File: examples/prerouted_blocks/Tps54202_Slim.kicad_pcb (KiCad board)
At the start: 2 copper layers, 9 parts

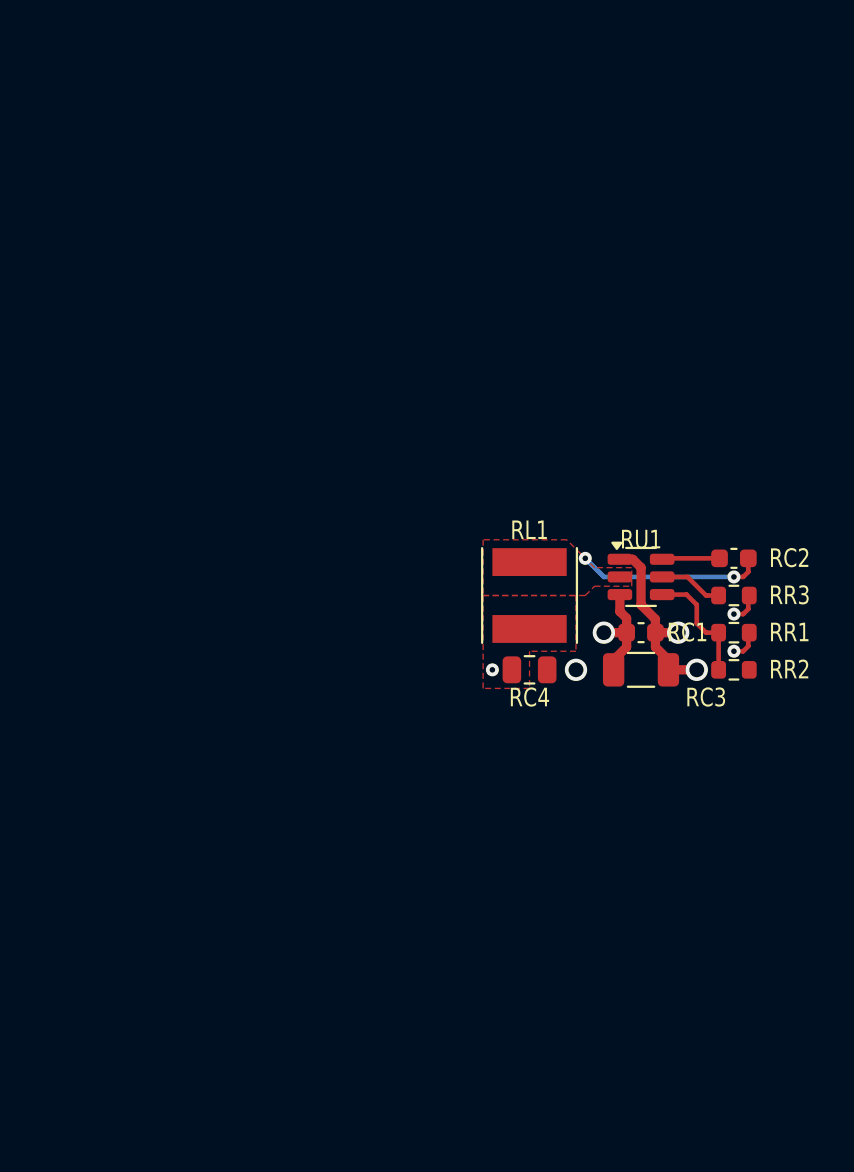
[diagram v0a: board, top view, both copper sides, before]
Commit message: clean up prerouted examples
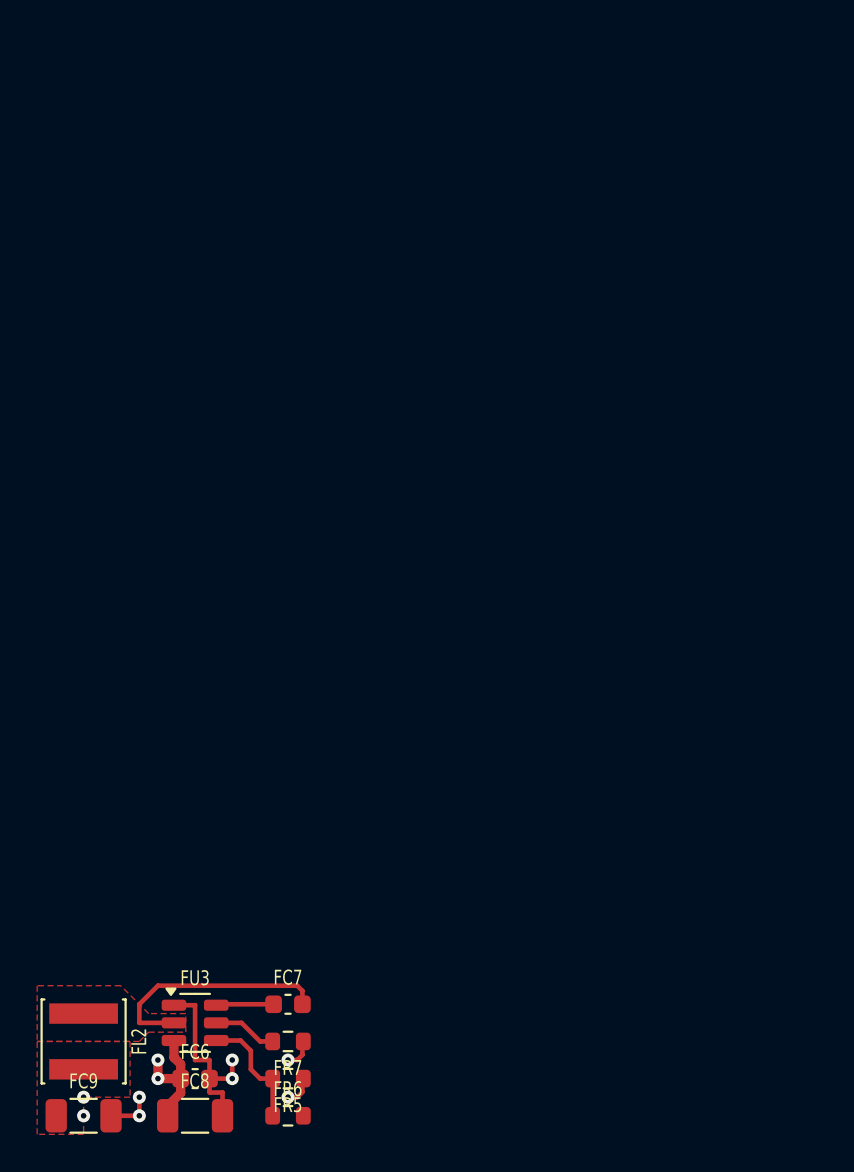
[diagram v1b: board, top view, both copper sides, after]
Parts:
- removed RC1, RC2: 50V 100nF X7R ±10% 0603 Multilayer Ceramic Capacitors MLCC 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, Capacitor_SMD:C_0603_1608Metric
- removed RC3: 50V 10uF X5R ±10% 1206 Multilayer Ceramic Capacitors MLCC -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, Capacitor_SMD:C_1206_3216Metric
- removed RC4: X5R 25V ±10% 10uF 0805 Multilayer Ceramic Capacitors MLCC -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, Capacitor_SMD:C_0805_2012Metric
- removed RL1: 1.4A 22uH ±20% 126m? SMD Power Inductors ROHS, Inductor_SMD:L_Taiyo-Yuden_NR-50xx
- removed RR1: ±1% 1/10W Thick Film Resistors 75V ±100ppm/? -55?~+155? 6.8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, Resistor_SMD:R_0603_1608Metric
- removed RR2: ±1% 1/10W Thick Film Resistors 75V ±100ppm/? -55?~+155? 1.5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, Resistor_SMD:R_0603_1608Metric
- removed RR3: ±1% 1/10W Thick Film Resistors 75V ±100ppm/? -55?~+155? 510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, Resistor_SMD:R_0603_1608Metric
- removed RU1: TPS54202H, Package_TO_SOT_SMD:SOT-23-6
- added FC6: reg_3v3.hf_in_cap, Capacitor_SMD:C_0603_1608Metric, F.Cu at (68.0, 134.0)
- added FC7: reg_3v3.boot_cap, Capacitor_SMD:C_0603_1608Metric, F.Cu at (73.0, 130.0)
- added FC8: reg_3v3.power_path.in_cap, Capacitor_SMD:C_1206_3216Metric, F.Cu at (68.0, 136.0)
- added FC9: reg_3v3.power_path.out_cap, Capacitor_SMD:C_1206_3216Metric, F.Cu at (62.0, 136.0)
- added FL2: reg_3v3.power_path.inductor, Inductor_SMD:L_Sunlord_SWPA4030S, F.Cu at (62.0, 132.0)
- added FR5: reg_3v3.fb.top_res, Resistor_SMD:R_0603_1608Metric, F.Cu at (73.0, 134.0)
- added FR6: reg_3v3.fb.bottom_res, Resistor_SMD:R_0603_1608Metric, F.Cu at (73.0, 136.0)
- added FR7: reg_3v3.en_res, Resistor_SMD:R_0603_1608Metric, F.Cu at (73.0, 132.0)
- added FU3: reg_3v3.ic, Package_TO_SOT_SMD:SOT-23-6, F.Cu at (68.0, 131.0)
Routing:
- net Fgnd: track 0.00 -> 13.3 mm, vias 0 -> 4
- net Freg_3v3.ic.sw: track 0.00 -> 12.9 mm
- net Rreg_3v3.boot_cap.neg: track 10.0 -> 0.00 mm, vias 2 -> 0
- net Rgnd: track 9.66 -> 0.00 mm, vias 3 -> 0
- net Fvin: track 0.00 -> 7.80 mm, vias 0 -> 3
- net Rvin: track 6.80 -> 0.00 mm, vias 2 -> 0
- net Freg_3v3.ic.fb: track 0.00 -> 6.47 mm
- net Rreg_3v3.fb.output: track 6.47 -> 0.00 mm
- net Rreg_3v3.en_res.b: track 3.45 -> 0.00 mm
- net Freg_3v3.ic.en: track 0.00 -> 3.45 mm
- net Rreg_3v3.boot_cap.pos: track 3.04 -> 0.00 mm
- net Freg_3v3.ic.boot: track 0.00 -> 3.04 mm
- net Rv3v3: track 1.61 -> 0.00 mm, vias 2 -> 0
- net Fv3v3: track 0.00 -> 1.61 mm, vias 0 -> 3
- added copper zone on F.Cu, net Freg_3v3.ic.sw
- added copper zone on F.Cu, net Fv3v3
- removed copper zone on F.Cu, net Rreg_3v3.boot_cap.neg
- removed copper zone on F.Cu, net Rv3v3

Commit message: wip converter layout
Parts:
- removed the FC6 at (68.0, 134.0)
- removed the FC8 at (68.0, 136.0)
- removed the FU3 at (68.0, 131.0)
- added FC6 (x2): reg_3v3.hf_in_cap, Capacitor_SMD:C_0603_1608Metric, F.Cu at (68.0, 134.0)
- added FC7: reg_3v3.boot_cap, Capacitor_SMD:C_0603_1608Metric, F.Cu at (72.0, 130.0)
- added FC8 (x2): reg_3v3.power_path.in_cap, Capacitor_SMD:C_1206_3216Metric, F.Cu at (68.0, 136.0)
- added FC9: reg_3v3.power_path.out_cap, Capacitor_SMD:C_1206_3216Metric, F.Cu at (63.0, 136.0)
- added FL2: reg_3v3.power_path.inductor, Inductor_SMD:L_Sunlord_SWPA4030S, F.Cu at (63.0, 132.0)
- added FR5: reg_3v3.fb.top_res, Resistor_SMD:R_0603_1608Metric, F.Cu at (72.0, 134.0)
- added FR6: reg_3v3.fb.bottom_res, Resistor_SMD:R_0603_1608Metric, F.Cu at (72.0, 136.0)
- added FR7: reg_3v3.en_res, Resistor_SMD:R_0603_1608Metric, F.Cu at (72.0, 132.0)
- added FU3 (x2): reg_3v3.ic, Package_TO_SOT_SMD:SOT-23-6, F.Cu at (68.0, 131.0)
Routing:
- net Fvin: track 7.80 -> 20.9 mm, vias 3 -> 6
- net Freg_3v3.ic.sw: track 12.9 -> 24.8 mm
- net Fv3v3: track 1.61 -> 12.6 mm, vias 3 -> 6
- net Fgnd: track 13.3 -> 24.1 mm, vias 4 -> 6
- net Freg_3v3.ic.fb: track 6.47 -> 12.0 mm
- net Freg_3v3.ic.en: track 3.45 -> 6.39 mm
- net Freg_3v3.ic.boot: track 3.04 -> 5.15 mm

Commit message: layout wip
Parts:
- removed FC6 (x2): reg_3v3.hf_in_cap, Capacitor_SMD:C_0603_1608Metric
- removed FC7 (x2): reg_3v3.boot_cap, Capacitor_SMD:C_0603_1608Metric
- removed FC8 (x2): reg_3v3.power_path.in_cap, Capacitor_SMD:C_1206_3216Metric
- removed FC9 (x2): reg_3v3.power_path.out_cap, Capacitor_SMD:C_1206_3216Metric
- removed FL2 (x2): reg_3v3.power_path.inductor, Inductor_SMD:L_Sunlord_SWPA4030S
- removed FR5 (x2): reg_3v3.fb.top_res, Resistor_SMD:R_0603_1608Metric
- removed FR6 (x2): reg_3v3.fb.bottom_res, Resistor_SMD:R_0603_1608Metric
- removed FR7 (x2): reg_3v3.en_res, Resistor_SMD:R_0603_1608Metric
- removed FU3 (x2): reg_3v3.ic, Package_TO_SOT_SMD:SOT-23-6
- added FC2: reg_5v.hf_in_cap, Capacitor_SMD:C_0603_1608Metric, F.Cu at (94.0, 88.0)
- added FC3: reg_5v.boot_cap, Capacitor_SMD:C_0603_1608Metric, F.Cu at (98.0, 84.0)
- added FC4: reg_5v.power_path.in_cap, Capacitor_SMD:C_1206_3216Metric, F.Cu at (94.0, 90.0)
- added FC5: reg_5v.power_path.out_cap, Capacitor_SMD:C_1206_3216Metric, F.Cu at (98.0, 80.0)
- added FL1: reg_5v.power_path.inductor, Inductor_SMD:L_Sunlord_SWPA3015S, F.Cu at (94.0, 80.0)
- added FR2: reg_5v.fb.top_res, Resistor_SMD:R_0603_1608Metric, F.Cu at (98.0, 86.0)
- added FR3: reg_5v.fb.bottom_res, Resistor_SMD:R_0603_1608Metric, F.Cu at (98.0, 88.0)
- added FR4: reg_5v.en_res, Resistor_SMD:R_0603_1608Metric, F.Cu at (98.0, 90.0)
- added FU2: reg_5v.ic, Package_TO_SOT_SMD:SOT-23-6, F.Cu at (94.0, 85.0)
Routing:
- net Freg_3v3.ic.sw: track 24.8 -> 0.00 mm
- net Fgnd: track 24.1 -> 7.96 mm, vias 6 -> 5
- net Fv5: track 0.00 -> 14.3 mm, vias 0 -> 2
- net Fv3v3: track 12.6 -> 0.00 mm, vias 6 -> 0
- net Freg_3v3.ic.fb: track 12.0 -> 0.00 mm
- net Fvin: track 20.9 -> 9.72 mm, vias 6 -> 2
- net Freg_5v.ic.sw: track 0.00 -> 10.3 mm
- net Freg_5v.ic.en: track 0.00 -> 7.91 mm
- net Freg_3v3.ic.en: track 6.39 -> 0.00 mm
- net Freg_3v3.ic.boot: track 5.15 -> 0.00 mm
- net Freg_5v.ic.fb: track 0.00 -> 4.06 mm
- net Freg_5v.ic.boot: track 0.00 -> 2.11 mm
- added copper zone on F.Cu, net Freg_5v.ic.sw
- added copper zone on F.Cu, net Fv5
- removed copper zone on F.Cu, net Freg_3v3.ic.sw
- removed copper zone on F.Cu, net Fv3v3
